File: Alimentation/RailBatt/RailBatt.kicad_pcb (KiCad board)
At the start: 2 copper layers, 82.2 x 12.2 mm, 8 parts, among them J1 Batt1, J2 Batt3, J3 Batt5, J4 Batt4, J5 Batt2, J6 Batt6

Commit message: Finalisation pour commande pack Alimentation 14/02/2021
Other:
- board text added: "JLCJLCJLCJLC"

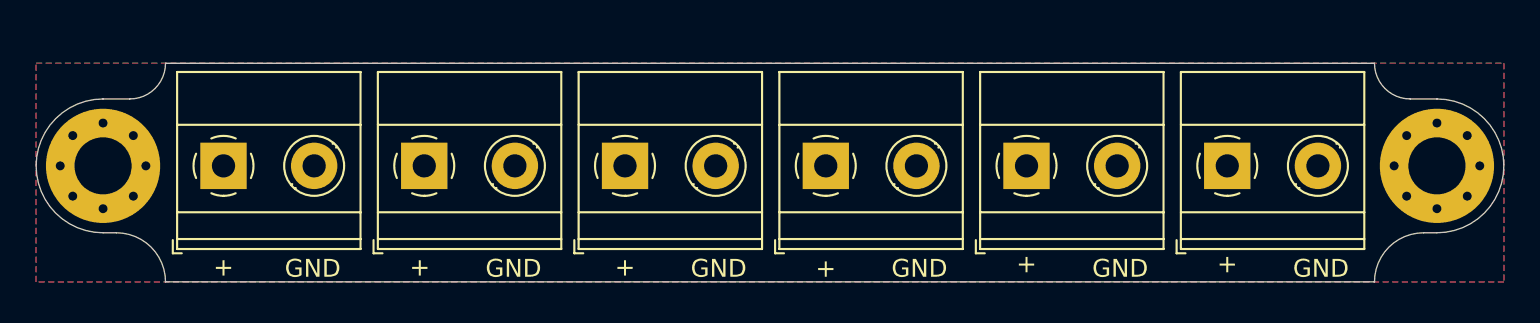
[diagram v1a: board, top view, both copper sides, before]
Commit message: Réduction de taille rail alimentation (fusion borniers)
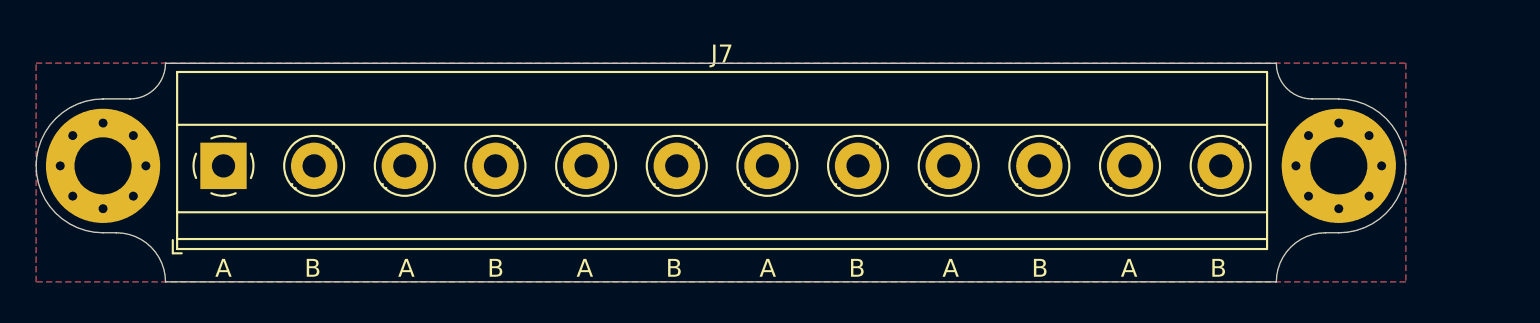
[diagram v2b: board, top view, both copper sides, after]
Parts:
- removed J1: Batt1, TerminalBlock_Phoenix:TerminalBlock_Phoenix_MKDS-1,5-2-5.08_1x02_P5.08mm_Horizontal
- removed J2: Batt3, TerminalBlock_Phoenix:TerminalBlock_Phoenix_MKDS-1,5-2-5.08_1x02_P5.08mm_Horizontal
- removed J3: Batt5, TerminalBlock_Phoenix:TerminalBlock_Phoenix_MKDS-1,5-2-5.08_1x02_P5.08mm_Horizontal
- removed J4: Batt4, TerminalBlock_Phoenix:TerminalBlock_Phoenix_MKDS-1,5-2-5.08_1x02_P5.08mm_Horizontal
- removed J5: Batt2, TerminalBlock_Phoenix:TerminalBlock_Phoenix_MKDS-1,5-2-5.08_1x02_P5.08mm_Horizontal
- removed J6: Batt6, TerminalBlock_Phoenix:TerminalBlock_Phoenix_MKDS-1,5-2-5.08_1x02_P5.08mm_Horizontal
- added J7: Screw_Terminal_01x12, TerminalBlock_Phoenix:TerminalBlock_Phoenix_MKDS-1,5-12-5.08_1x12_P5.08mm_Horizontal, F.Cu at (89.5, 85.0)
- moved H2 5.50 mm to (152.0, 85.0)
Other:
- board size 82.2 x 12.2 mm -> 76.8 x 12.2 mm
- board text added: "A"
- board text added: "B"
- board text removed: "+"
- board text removed: "GND"
